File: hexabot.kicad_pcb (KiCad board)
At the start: 2 copper layers, 0 parts

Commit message: Partial footprint association
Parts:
- added C1: 2u2, hexabot:R_0805_HandSoldering, F.Cu at (255.5, 136.2)
- added C10: 10u, hexabot:R_0805_HandSoldering, F.Cu at (232.4, 149.5)
- added C11: 100n, hexabot:R_0805_HandSoldering, F.Cu at (287.5, 90.9)
- added C12: 100n, hexabot:R_0805_HandSoldering, F.Cu at (282.3, 97.2)
- added C13: 100n, hexabot:R_0805_HandSoldering, F.Cu at (255.8, 123.6)
- added C14: 100n, hexabot:R_0805_HandSoldering, F.Cu at (270.4, 110.7)
- added C15: 100n, hexabot:R_0805_HandSoldering, F.Cu at (250.2, 126.1)
- added C16: 100n, hexabot:R_0805_HandSoldering, F.Cu at (317.9, 103.9)
- added C17: 15n, hexabot:R_0805_HandSoldering, F.Cu at (323.2, 97.2)
- added C18: 22n, hexabot:R_0805_HandSoldering, F.Cu at (317.9, 97.6)
- added C19: 15n, hexabot:R_0805_HandSoldering, F.Cu at (325.0, 90.9)
- added C2: 2u2, hexabot:R_0805_HandSoldering, F.Cu at (184.0, 149.8)
- added C20: 220n, hexabot:R_0805_HandSoldering, F.Cu at (312.7, 103.9)
- added C21: 100n, hexabot:R_0805_HandSoldering, F.Cu at (319.7, 114.0)
- added C22: 15n, hexabot:R_0805_HandSoldering, F.Cu at (312.7, 120.7)
- added C23: 22n, hexabot:R_0805_HandSoldering, F.Cu at (317.9, 120.7)
- added C24: 15n, hexabot:R_0805_HandSoldering, F.Cu at (323.2, 120.3)
- added C25: 220n, hexabot:R_0805_HandSoldering, F.Cu at (317.9, 127.0)
- added C26: NC, hexabot:R_0805_HandSoldering, F.Cu at (242.9, 149.4)
- added C3: 100n, hexabot:R_0805_HandSoldering, F.Cu at (189.3, 149.8)
- added C4: 330u, hexabot:c_elec_8x10.5, F.Cu at (232.6, 119.1)
- added C5: 330u, hexabot:c_elec_10x10.5, F.Cu at (187.6, 139.8)
- added C6: 4u7, hexabot:R_0805_HandSoldering, F.Cu at (227.2, 139.9)
- added C7: 18p, hexabot:R_0805_HandSoldering, F.Cu at (227.2, 146.2)
- added C8: 18p, hexabot:R_0805_HandSoldering, F.Cu at (282.3, 90.9)
- added C9: 4u7, hexabot:R_0805_HandSoldering, F.Cu at (253.4, 148.8)
- added JP1: JUMPER, Pin_Headers:Pin_Header_Straight_1x02, F.Cu at (241.0, 119.4)
- added JP2: JUMPER, Pin_Headers:Pin_Header_Straight_1x02, F.Cu at (266.2, 93.9)
- added JP3: JUMPER, Pin_Headers:Pin_Header_Straight_1x02, F.Cu at (250.0, 118.4)
- added P10: BUMP2, Sockets_MOLEX_KK-System:Socket_MOLEX-KK-RM2-54mm_Lock_2pin_straight, F.Cu at (220.9, 130.6)
- added P11: USB_B, hexabot:MICRO-B_USB, F.Cu at (242.7, 130.7)
- added P12: DEBUG, Pin_Headers:Pin_Header_Straight_1x05, F.Cu at (213.9, 114.8)
- added P13: NC, Sockets_MOLEX_KK-System:Socket_MOLEX-KK-RM2-54mm_Lock_5pin_straight, F.Cu at (249.1, 93.8)
- added P14: MOTOR_R, Sockets_MOLEX_KK-System:Socket_MOLEX-KK-RM2-54mm_Lock_2pin_straight, F.Cu at (260.0, 93.2)
- added P15: MOTOR_L, Sockets_MOLEX_KK-System:Socket_MOLEX-KK-RM2-54mm_Lock_2pin_straight, F.Cu at (221.6, 142.2)
- added P16: UART1_5V, Sockets_MOLEX_KK-System:Socket_MOLEX-KK-RM2-54mm_Lock_4pin_straight, F.Cu at (252.2, 106.1)
- added P17: ENC1, Sockets_MOLEX_KK-System:Socket_MOLEX-KK-RM2-54mm_Lock_4pin_straight, F.Cu at (209.9, 146.4)
- added P18: ENC2, Sockets_MOLEX_KK-System:Socket_MOLEX-KK-RM2-54mm_Lock_4pin_straight, F.Cu at (222.0, 119.0)
- added P19: ENC3, Sockets_MOLEX_KK-System:Socket_MOLEX-KK-RM2-54mm_Lock_4pin_straight, F.Cu at (241.4, 107.1)
- added P20: ENC4, Sockets_MOLEX_KK-System:Socket_MOLEX-KK-RM2-54mm_Lock_4pin_straight, F.Cu at (199.2, 139.0)
- added P21: UART2_3V3, Pin_Headers:Pin_Header_Straight_1x06, F.Cu at (177.1, 139.1)
- added P22: NC, Sockets_MOLEX_KK-System:Socket_MOLEX-KK-RM2-54mm_Lock_6pin_straight, F.Cu at (228.3, 93.8)
- added P23: START, Sockets_MOLEX_KK-System:Socket_MOLEX-KK-RM2-54mm_Lock_2pin_straight, F.Cu at (233.1, 130.5)
- added P25: NC, Pin_Headers:Pin_Header_Straight_1x01, F.Cu at (195.8, 151.3)
- added P26: NC, Pin_Headers:Pin_Header_Straight_1x01, F.Cu at (255.2, 118.4)
- added P27: NC, Pin_Headers:Pin_Header_Straight_1x01, F.Cu at (199.7, 151.3)
- added P3: SERVO1, Pin_Headers:Pin_Header_Straight_1x03, F.Cu at (214.3, 133.2)
- added P4: SERVO2, Pin_Headers:Pin_Header_Straight_1x03, F.Cu at (239.3, 93.9)
- added P6: PICKIT, Pin_Headers:Pin_Header_Straight_1x05, F.Cu at (217.8, 93.9)
- added P8: NC, Pin_Headers:Pin_Header_Straight_1x06, F.Cu at (213.2, 93.9)
- added P9: BUMP1, Sockets_MOLEX_KK-System:Socket_MOLEX-KK-RM2-54mm_Lock_2pin_straight, F.Cu at (227.2, 130.6)
- added Q1: Q_NMOS_GSD, Housings_SOT-23_SOT-143_TSOT-6:SOT-23_Handsoldering, F.Cu at (235.2, 141.5)
- added Q2: Q_NMOS_GSD, Housings_SOT-23_SOT-143_TSOT-6:SOT-23_Handsoldering, F.Cu at (262.6, 113.9)
- added Q3: Q_NMOS_GSD, Housings_SOT-23_SOT-143_TSOT-6:SOT-23_Handsoldering, F.Cu at (262.6, 104.2)
- added Q4: Q_NMOS_GSD, Housings_SOT-23_SOT-143_TSOT-6:SOT-23_Handsoldering, F.Cu at (274.5, 92.6)
- added R1: 4K7, hexabot:R_0805_HandSoldering, F.Cu at (260.7, 140.8)
- added R10: NC, hexabot:R_0805_HandSoldering, F.Cu at (255.5, 129.9)
- added R11: NC, hexabot:R_0805_HandSoldering, F.Cu at (250.2, 132.4)
- added R12: 9k, hexabot:R_0805_HandSoldering, F.Cu at (248.2, 138.7)
- added R13: NC, hexabot:R_0805_HandSoldering, F.Cu at (286.1, 116.1)
- added R14: NC, hexabot:R_0805_HandSoldering, F.Cu at (266.0, 135.9)
- added R15: NC, hexabot:R_0805_HandSoldering, F.Cu at (276.8, 123.3)
- added R16: 1k, hexabot:R_0805_HandSoldering, F.Cu at (271.6, 129.6)
- added R17: 0R, hexabot:R_0805_HandSoldering, F.Cu at (207.1, 136.1)
- added R18: 0R, hexabot:R_0805_HandSoldering, F.Cu at (260.7, 134.5)
- added R19: 470R, hexabot:R_0805_HandSoldering, F.Cu at (286.1, 109.8)
- added R2: 21k, hexabot:R_0805_HandSoldering, F.Cu at (237.7, 149.5)
- added R20: 470R, hexabot:R_0805_HandSoldering, F.Cu at (280.9, 116.1)
- added R21: 470R, hexabot:R_0805_HandSoldering, F.Cu at (248.2, 148.8)
- added R22: 10k, hexabot:R_0805_HandSoldering, F.Cu at (266.3, 129.6)
- added R23: 2k, hexabot:R_0805_HandSoldering, F.Cu at (261.1, 128.2)
- added R24: 1k, hexabot:R_0805_HandSoldering, F.Cu at (271.6, 123.3)
- added R25: 470R, hexabot:R_0805_HandSoldering, F.Cu at (253.4, 142.5)
- added R26: 10k, hexabot:R_0805_HandSoldering, F.Cu at (266.3, 123.3)
- added R27: 10k, hexabot:R_0805_HandSoldering, F.Cu at (242.9, 136.8)
- added R28: 1k, hexabot:R_0805_HandSoldering, F.Cu at (275.6, 117.0)
- added R29: 10R, hexabot:R_0805_HandSoldering, F.Cu at (319.7, 90.9)
- added R3: 7k52, hexabot:R_0805_HandSoldering, F.Cu at (283.6, 103.5)
- added R30: 10k, hexabot:R_0805_HandSoldering, F.Cu at (312.7, 97.6)
- added R31: 0R1 3W, hexabot:R_1206_HandSoldering, F.Cu at (313.6, 91.1)
- added R32: 10R, hexabot:R_0805_HandSoldering, F.Cu at (312.7, 127.0)
- added R33: 10k, hexabot:R_0805_HandSoldering, F.Cu at (325.0, 114.0)
- added R34: 0R1 3W, hexabot:R_1206_HandSoldering, F.Cu at (313.6, 114.2)
- added R35: 1k, hexabot:R_0805_HandSoldering, F.Cu at (280.9, 109.8)
- added R4: 330R, hexabot:R_0805_HandSoldering, F.Cu at (278.3, 103.5)
- added R5: 10k, hexabot:R_0805_HandSoldering, F.Cu at (287.5, 97.2)
- added R6: 10k, hexabot:R_0805_HandSoldering, F.Cu at (261.1, 121.9)
- added R7: 10k, hexabot:R_0805_HandSoldering, F.Cu at (270.4, 117.0)
- added R8: 1M, hexabot:R_0805_HandSoldering, F.Cu at (275.6, 110.7)
- added R9: NC, hexabot:R_0805_HandSoldering, F.Cu at (242.9, 143.1)
- added U1: PTN78020 +5V, hexabot:PTN78020H, F.Cu at (192.0, 98.9)
- added U2: PTN78020 SERVO, hexabot:PTN78020H, F.Cu at (192.0, 121.5)
- added U3: MCP1727, hexabot:SOIC-8_3.9x4.9mm_Pitch1.27mm, F.Cu at (271.7, 103.0)
- added U5: L6201PS, hexabot:powerso-20, F.Cu at (301.7, 95.5)
- added U6: L6201PS, hexabot:powerso-20, F.Cu at (301.7, 118.7)
- added Y1: 8M, hexabot:Crystal_HC49-SD_SMD, F.Cu at (228.2, 106.7)

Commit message: Draft layout with files
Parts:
- added D1: D, hexabot:SOD-128, F.Cu at (185.0, 114.0)
- added D10: LEDB, Resistors_SMD:R_0805, F.Cu at (103.5, 90.0)
- added D11: D, Diodes_SMD:SOD-123, F.Cu at (174.0, 49.0)
- added D12: D, Diodes_SMD:SOD-123, F.Cu at (186.0, 49.0)
- added D13: D, Diodes_SMD:SOD-123, F.Cu at (113.0, 49.0)
- added D14: D, Diodes_SMD:SOD-123, F.Cu at (127.0, 49.0)
- added D2: ZENER, Diodes_SMD:SOD-323, F.Cu at (141.8, 119.2)
- added D3: ZENER, Diodes_SMD:SOD-323, B.Cu at (159.8, 104.0)
- added D4: LEDR, Resistors_SMD:R_0805, F.Cu at (155.0, 149.5)
- added D5: LEDY, Resistors_SMD:R_0805, F.Cu at (160.0, 149.5)
- added D6: LEDG, Resistors_SMD:R_0805, F.Cu at (157.5, 149.5)
- added D7: LEDB, Resistors_SMD:R_0805, F.Cu at (79.0, 96.2)
- added D8: LEDB, Resistors_SMD:R_0805, F.Cu at (88.2, 98.2)
- added D9: LEDB, Resistors_SMD:R_0805, F.Cu at (103.5, 98.0)
- added F1: FUSE, Resistors_SMD:R_1206_HandSoldering, F.Cu at (185.0, 105.0)
- added MH1: HOLE_M3, hexabot:M3-hole-plated, F.Cu at (277.0, 157.0)
- added MH2: HOLE_M3, hexabot:M3-hole-plated, F.Cu at (104.0, 44.0)
- added MH3: HOLE_M3, hexabot:M3-hole-plated, F.Cu at (270.0, 157.0)
- added MH4: HOLE_M3, hexabot:M3-hole-plated, F.Cu at (196.0, 44.0)
- added P1: BATTERY, Sockets_MOLEX_KK-System:Socket_MOLEX-KK-RM3-96mm_Lock_2pin_straight, F.Cu at (194.0, 123.0)
- added P2: EXT_POWER, Sockets_MOLEX_KK-System:Socket_MOLEX-KK-RM3-96mm_Lock_2pin_straight, F.Cu at (194.0, 114.0)
- added P24: DYNAMIXEL2, Pin_Headers:Pin_Header_Straight_1x03, F.Cu at (171.0, 131.0)
- added P5: DYNAMIXEL1, Pin_Headers:Pin_Header_Straight_1x03, F.Cu at (171.0, 136.0)
- added P7: PANIC BUTTON, Sockets_MOLEX_KK-System:Socket_MOLEX-KK-RM3-96mm_Lock_2pin_straight, F.Cu at (194.0, 105.0)
- added SW1: PUSH1, hexabot:SW_PUSH-SMD, F.Cu at (152.8, 140.5)
- added SW2: PUSH2, hexabot:SW_PUSH-SMD, F.Cu at (159.8, 140.5)
- added U4: DSPIC33EP256MU806, hexabot:QFN-64-1EP_9x9mm_Pitch0.5mm, F.Cu at (137.5, 130.8)
- C1, C17, C18, C19, C2, C22, C23, C24, C26, C6, C9, R2, R26, R27, R29, R3, R32, R35, R5, R6, R7: footprint hexabot:R_0805_HandSoldering -> Resistors_SMD:R_0805; moved to B.Cu
- C10, C11, C12, C13, C14, C15, C16, C20, C21, C25, C3, C7, C8, R1, R10, R11, R12, R13, R14, R15, R16, R17, R18, R19, R20, R21, R22, R23, R24, R25, R28, R30, R33, R4, R8, R9: footprint hexabot:R_0805_HandSoldering -> Resistors_SMD:R_0805
- P12: footprint Pin_Headers:Pin_Header_Straight_1x05 -> Sockets_MOLEX_KK-System:Socket_MOLEX-KK-RM2-54mm_Lock_5pin_straight
- P14, P15: footprint Sockets_MOLEX_KK-System:Socket_MOLEX-KK-RM2-54mm_Lock_2pin_straight -> Sockets_MOLEX_KK-System:Socket_MOLEX-KK-RM3-96mm_Lock_2pin_straight
- P21: value UART2_3V3 -> UART2_FTDI3V3
- Q1, Q2, Q3: footprint Housings_SOT-23_SOT-143_TSOT-6:SOT-23_Handsoldering -> Housings_SOT-23_SOT-143_TSOT-6:SOT-23; moved to B.Cu
- Q4: footprint Housings_SOT-23_SOT-143_TSOT-6:SOT-23_Handsoldering -> Housings_SOT-23_SOT-143_TSOT-6:SOT-23
- R31, R34: footprint hexabot:R_1206_HandSoldering -> Resistors_SMD:R_0805
- U3: moved to B.Cu
- moved C23 214.9 mm to (118.0, 42.0), turned to 180 degrees
- moved C24 212.7 mm to (125.0, 43.0), turned to 90 degrees
- moved C22 212.4 mm to (115.0, 43.0), turned to 90 degrees
- moved R32 208.8 mm to (122.0, 42.0)
- moved C25 203.2 mm to (122.0, 73.0), turned to 270 degrees
- moved R33 201.2 mm to (128.0, 73.0), turned to 90 degrees
- moved C21 196.1 mm to (133.0, 54.0), turned to 270 degrees
- moved R34 193.0 mm to (125.0, 73.0), turned to 90 degrees
- moved R16 190.1 mm to (85.8, 89.5), turned to 180 degrees
- moved U6 186.6 mm to (124.0, 62.0), turned to 180 degrees
- moved R22 180.0 mm to (91.0, 89.0), turned to 180 degrees
- moved Q4 176.7 mm to (107.2, 149.5), turned to 180 degrees
- moved R4 174.6 mm to (103.8, 102.5)
- moved R28 167.8 mm to (111.0, 149.5), turned to 270 degrees
- moved C11 167.0 mm to (124.8, 128.0)
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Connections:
- P14 pad 1: /DRIVER_R/OUT1 -> /DRIVER_R/OUT2
- P14 pad 2: /DRIVER_R/OUT2 -> /DRIVER_R/OUT1
- P15 pad 1: /DRIVER_L/OUT1 -> /DRIVER_L/OUT2
- P15 pad 2: /DRIVER_L/OUT2 -> /DRIVER_L/OUT1
- P22 pad 2: /SCL -> /SDA
- P22 pad 3: /SDA -> /SCL
- R26 pad 2: /SDA -> /SCL
- R27 pad 1: /SCL -> /SDA
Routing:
- net /DRIVER_L/MOTOR_POWER: track 0.00 -> 191.7 mm, vias 0 -> 3
- net GND: track 0.00 -> 133.2 mm
- net /ENC_2_A: track 0.00 -> 119.1 mm, vias 0 -> 2
- net /ENC_2_B: track 0.00 -> 116.9 mm, vias 0 -> 2
- net /DRIVER_L/DIR1: track 0.00 -> 110.5 mm, vias 0 -> 2
- net /ENC_4_B: track 0.00 -> 109.6 mm
- net /ENC_4_A: track 0.00 -> 109.3 mm
- net /DRIVER_R/DIR1: track 0.00 -> 107.0 mm, vias 0 -> 4
- net +BATT: track 0.00 -> 101.6 mm, vias 0 -> 2
- net /DRIVER_R/PWM: track 0.00 -> 99.4 mm, vias 0 -> 2
- net /ENC_3_B: track 0.00 -> 94.2 mm
- net +5V: track 0.00 -> 94.1 mm, vias 0 -> 1
- net /ENC_3_A: track 0.00 -> 92.9 mm
- net /DRIVER_L/DIR2: track 0.00 -> 91.2 mm, vias 0 -> 2
- net /DRIVER_R/DIR2: track 0.00 -> 88.0 mm, vias 0 -> 2
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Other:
- board outline added: 100 x 105 mm
- net class Default: trace_width 0.25 -> 0.29
- net class mid_power added: clearance 0.2, trace_width 0.5, via_dia 1, via_drill 0.5
- net class power added: clearance 0.2, trace_width 0.8, via_dia 1.2, via_drill 0.6

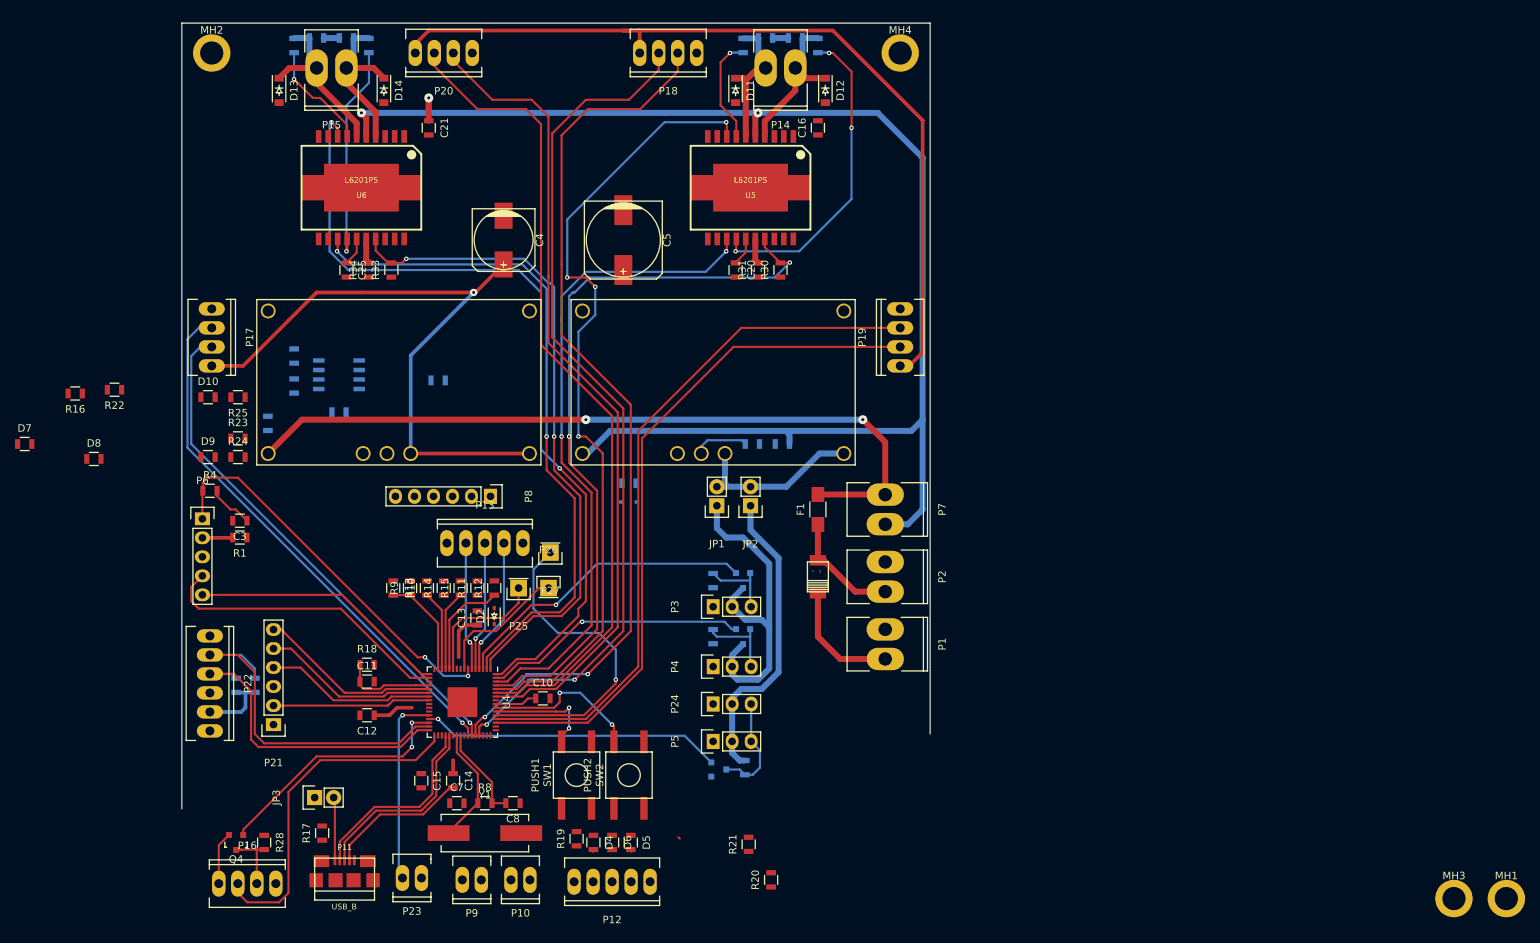
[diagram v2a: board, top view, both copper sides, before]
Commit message: Layout nearly done, ground plane to check, missing connections, change quartz footprint
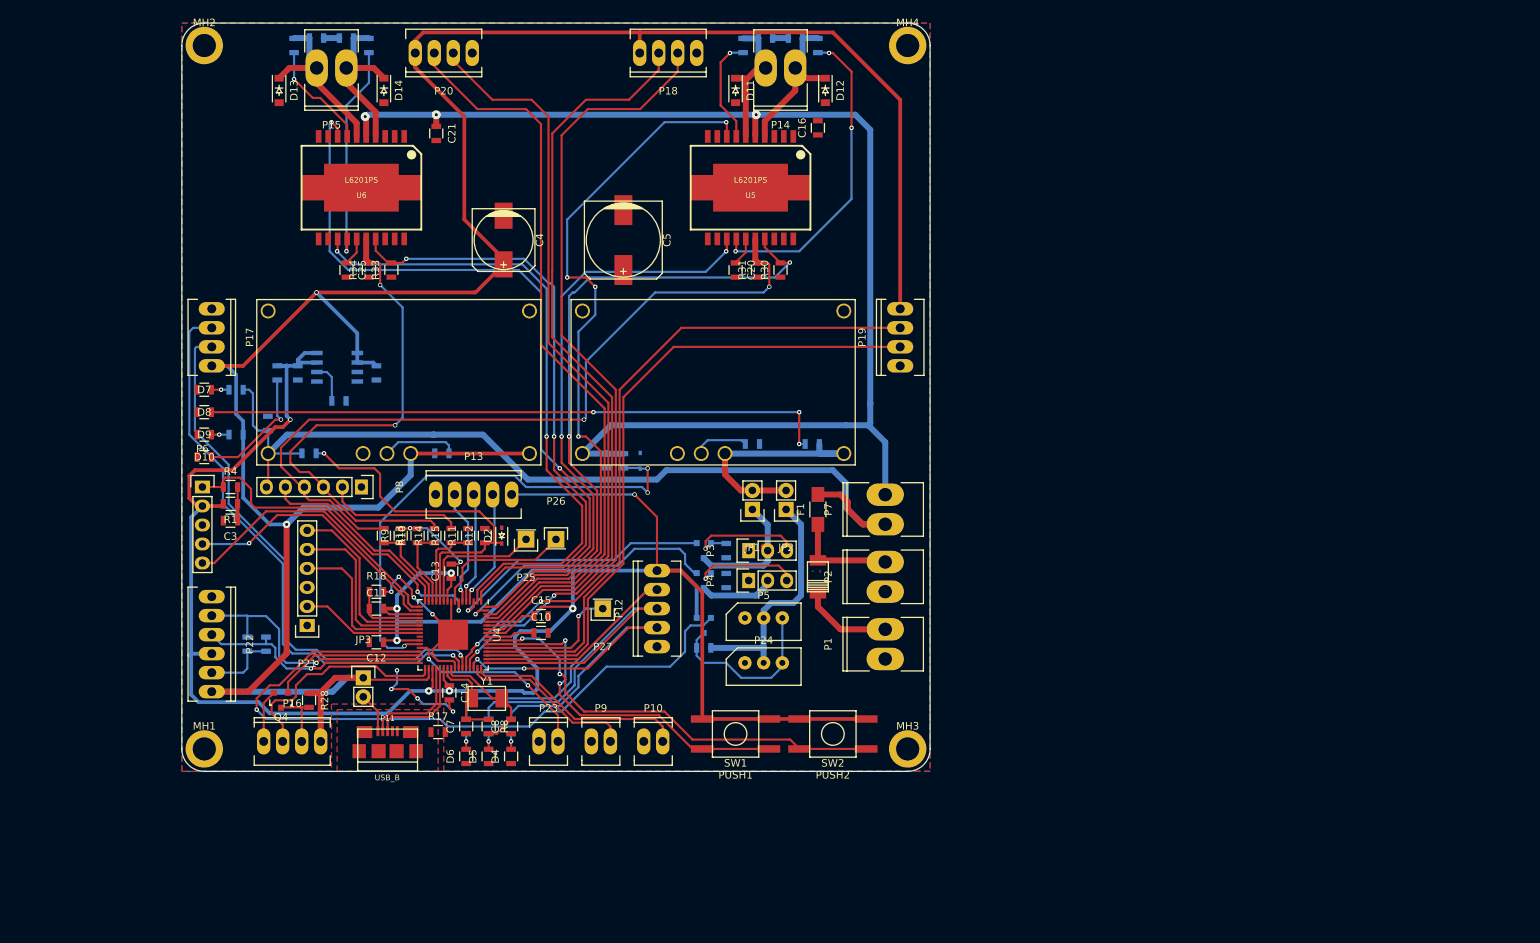
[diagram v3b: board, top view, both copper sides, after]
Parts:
- P24, P5: footprint Pin_Headers:Pin_Header_Straight_1x03 -> hexabot:molex-22-03-5035
- R16, R19, R20, R21, R22, R23, R24, R25: moved to B.Cu
- Y1: footprint hexabot:Crystal_HC49-SD_SMD -> Crystal_SMD_5x3.2mm
- moved MH1 175.1 mm to (103.0, 137.0)
- moved R23 76.8 mm to (184.2, 96.2), turned to 180 degrees
- moved MH3 75.7 mm to (197.0, 137.0)
- moved R20 43.0 mm to (141.0, 134.0), turned to 270 degrees
- moved R21 40.9 mm to (138.0, 134.0), turned to 270 degrees
- moved P12 37.0 mm to (163.5, 118.2), turned to 90 degrees
- moved R16 32.3 mm to (117.0, 97.5)
- moved SW2 27.8 mm to (187.0, 135.0), turned to 180 degrees
- moved C15 27.2 mm to (148.0, 119.2), turned to 0 degrees
- moved P23 25.8 mm to (149.0, 136.0), turned to 0 degrees
- moved P10 25.6 mm to (163.0, 136.0), turned to 0 degrees
- moved P9 25.3 mm to (156.0, 136.0), turned to 0 degrees
- moved D7 25.1 mm to (103.0, 89.0)
- moved C2 23.6 mm to (156.8, 98.5), turned to 270 degrees
- moved D6 22.6 mm to (138.0, 138.0), turned to 90 degrees
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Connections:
- P12 pad 2: /LEDG -> /LEDR
- P12 pad 4: /LEDR -> /LEDG
- P8 pad 2: /VREF -> /AN3_FULL
- P8 pad 3: /DRIVER_R/SENSE -> /DRIVER_L/SENSE
- P8 pad 4: /DRIVER_L/SENSE -> /DRIVER_R/SENSE
- P8 pad 5: /AN3_FULL -> /VREF
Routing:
- net +3V3: track 18.2 -> 314.3 mm, vias 0 -> 8
- net +5V: track 94.1 -> 336.0 mm, vias 1 -> 2
- net /DRIVER_R/SENSE: track 3.35 -> 106.8 mm, vias 0 -> 2
- net Net-(D8-Pad2): track 0.00 -> 83.6 mm, vias 0 -> 3
- net GND: track 133.2 -> 62.8 mm, vias 0 -> 10
- net /~PANIC: track 0.00 -> 68.1 mm, vias 0 -> 3
- net /DRIVER_L/SENSE: track 3.35 -> 68.4 mm, vias 0 -> 2
- net /LEDG: track 0.00 -> 61.4 mm
- net /LEDY: track 0.00 -> 56.7 mm
- net /DYNAMIXEL: track 40.1 -> 95.1 mm
- net /LEDR: track 0.00 -> 54.4 mm, vias 0 -> 2
- net /PUSH_2: track 21.3 -> 59.3 mm
- net /PUSH_1: track 15.0 -> 49.4 mm
- net /AN4: track 13.9 -> 47.5 mm, vias 0 -> 1
- net /BUMP_2: track 0.00 -> 29.8 mm
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- added copper zone on F.Cu, net /USB_SHIELD
- added copper zone on B.Cu, net GND
- added copper zone on F.Cu, net GND
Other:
- board size 100 x 105 mm -> 100 x 100 mm
